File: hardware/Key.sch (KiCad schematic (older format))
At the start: 2 parts

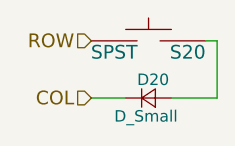
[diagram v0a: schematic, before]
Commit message: Add HWB, breakouts, LED to sch
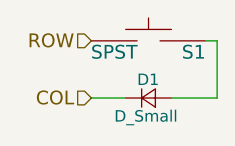
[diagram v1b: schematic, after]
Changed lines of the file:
@@
 $Descr A4 11693 8268
 encoding utf-8
-Sheet 22 66
+Sheet 6 66
 Title ""
 Date ""
@@
 AR Path="/5947FBED/594A0FA7/5940D01B" Ref="S63"  Part="1"
 AR Path="/5947FBED/594A0FB1/5940D01B" Ref="S64"  Part="1"
-F 0 "S20" H 2900 1750 60  0000 R CNN
+F 0 "S1" H 2900 1750 60  0000 R CNN
 F 1 "SPST" H 2500 1750 60  0000 C CNN
 F 2 "keyboard-modules:CHERRY_PCB_100H" H 2650 1900 60  0001 C CNN
@@
 AR Path="/5947FBED/594A0FA7/5940D05E" Ref="D63"  Part="1"
 AR Path="/5947FBED/594A0FB1/5940D05E" Ref="D64"  Part="1"
-F 0 "D20" H 2600 2130 50  0000 L CNN
+F 0 "D1" H 2600 2130 50  0000 L CNN
 F 1 "D_Small" H 2500 1970 50  0000 L CNN
 F 2 "Diodes_SMD:D_1206" V 2650 2050 50  0001 C CNN

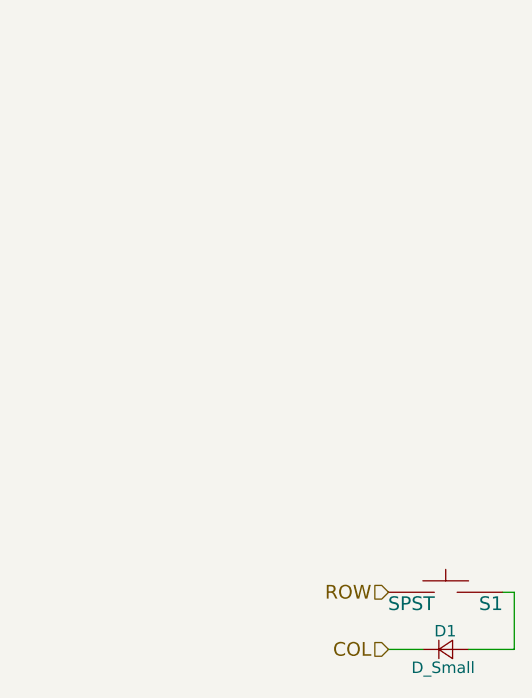
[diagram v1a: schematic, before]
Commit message: Move diodes in script, add big thumb buttons
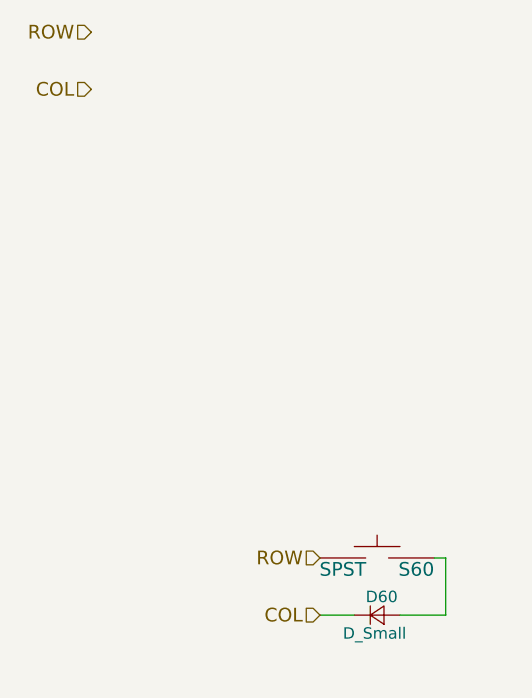
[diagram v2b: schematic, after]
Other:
- moved on the sheet: D60, S60
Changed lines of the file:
@@
 Comment4 ""
 $EndDescr
-Text HLabel 2400 1800 0    60   Input ~ 0
+Text HLabel 2100 1650 0    60   Input ~ 0
 ROW
-Text HLabel 2400 2050 0    60   Input ~ 0
+Text HLabel 2100 1900 0    60   Input ~ 0
 COL
 $Comp
 L SPST S1
 U 1 1 5940D01B
-P 2650 1800
+P 2350 1650
 AR Path="/5947FBED/594A0D2A/5940D01B" Ref="S1"  Part="1"
 AR Path="/5947FBED/594A0D35/5940D01B" Ref="S2"  Part="1"
@@
 AR Path="/5947FBED/594A0F7E/5940D01B" Ref="S59"  Part="1"
 AR Path="/5947FBED/594A0F88/5940D01B" Ref="S60"  Part="1"
-AR Path="/5947FBED/594A0F93/5940D01B" Ref="S61"  Part="1"
-AR Path="/5947FBED/594A0F9D/5940D01B" Ref="S62"  Part="1"
-AR Path="/5947FBED/594A0FA7/5940D01B" Ref="S63"  Part="1"
-AR Path="/5947FBED/594A0FB1/5940D01B" Ref="S64"  Part="1"
-F 0 "S1" H 2900 1750 60  0000 R CNN
-F 1 "SPST" H 2500 1750 60  0000 C CNN
-F 2 "keyboard-modules:CHERRY_PCB_100H" H 2650 1900 60  0001 C CNN
-F 3 "" H 2650 1900 60  0001 C CNN
-	1    2650 1800
+F 0 "S60" H 2600 1600 60  0000 R CNN
+F 1 "SPST" H 2200 1600 60  0000 C CNN
+F 2 "keyboard-modules:CHERRY_PCB_100H" H 2350 1750 60  0001 C CNN
+F 3 "" H 2350 1750 60  0001 C CNN
+	1    2350 1650
 	1    0    0    -1
 $EndComp
@@
 L D_Small D1
 U 1 1 5940D05E
-P 2650 2050
+P 2350 1900
 AR Path="/5947FBED/594A0D2A/5940D05E" Ref="D1"  Part="1"
 AR Path="/5947FBED/594A0D35/5940D05E" Ref="D2"  Part="1"
@@
 AR Path="/5947FBED/594A0F7E/5940D05E" Ref="D59"  Part="1"
 AR Path="/5947FBED/594A0F88/5940D05E" Ref="D60"  Part="1"
-AR Path="/5947FBED/594A0F93/5940D05E" Ref="D61"  Part="1"
-AR Path="/5947FBED/594A0F9D/5940D05E" Ref="D62"  Part="1"
-AR Path="/5947FBED/594A0FA7/5940D05E" Ref="D63"  Part="1"
-AR Path="/5947FBED/594A0FB1/5940D05E" Ref="D64"  Part="1"
-F 0 "D1" H 2600 2130 50  0000 L CNN
-F 1 "D_Small" H 2500 1970 50  0000 L CNN
-F 2 "Diodes_SMD:D_1206" V 2650 2050 50  0001 C CNN
-F 3 "" V 2650 2050 50  0001 C CNN
-	1    2650 2050
+F 0 "D60" H 2300 1980 50  0000 L CNN
+F 1 "D_Small" H 2200 1820 50  0000 L CNN
+F 2 "Diodes_SMD:D_1206" V 2350 1900 50  0001 C CNN
+F 3 "" V 2350 1900 50  0001 C CNN
+	1    2350 1900
 	1    0    0    -1
 $EndComp
 Wire Wire Line
-	2400 2050 2550 2050
+	2100 1900 2250 1900
 Wire Wire Line
-	2900 1800 2950 1800
+	2600 1650 2650 1650
 Wire Wire Line
-	2950 1800 2950 2050
+	2650 1650 2650 1900
 Wire Wire Line
-	2950 2050 2750 2050
+	2650 1900 2450 1900
+Text HLabel 1100 -650 0    60   Input ~ 0
+ROW
+Text HLabel 1100 -400 0    60   Input ~ 0
+COL
 $EndSCHEMATC

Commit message: Fix diodes, Add board edge
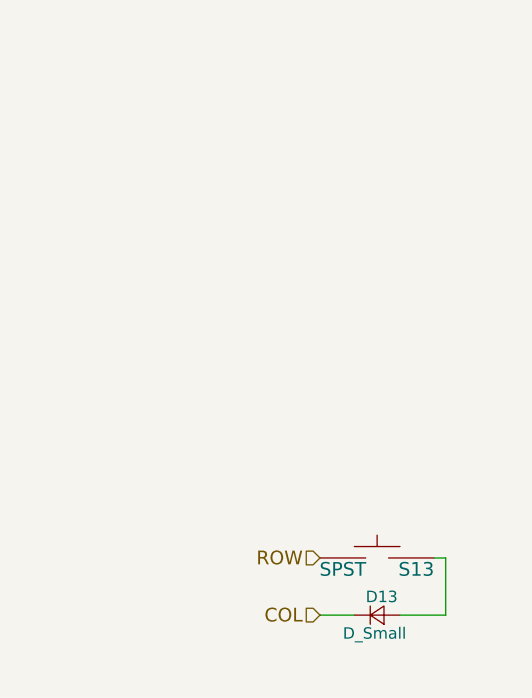
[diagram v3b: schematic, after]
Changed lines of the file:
@@
 $Descr A4 11693 8268
 encoding utf-8
-Sheet 6 66
+Sheet 15 66
 Title ""
 Date ""
@@
 AR Path="/5947FBED/594A0F7E/5940D01B" Ref="S59"  Part="1"
 AR Path="/5947FBED/594A0F88/5940D01B" Ref="S60"  Part="1"
-F 0 "S60" H 2600 1600 60  0000 R CNN
+F 0 "S13" H 2600 1600 60  0000 R CNN
 F 1 "SPST" H 2200 1600 60  0000 C CNN
 F 2 "keyboard-modules:CHERRY_PCB_100H" H 2350 1750 60  0001 C CNN
@@
 AR Path="/5947FBED/594A0F7E/5940D05E" Ref="D59"  Part="1"
 AR Path="/5947FBED/594A0F88/5940D05E" Ref="D60"  Part="1"
-F 0 "D60" H 2300 1980 50  0000 L CNN
+F 0 "D13" H 2300 1980 50  0000 L CNN
 F 1 "D_Small" H 2200 1820 50  0000 L CNN
 F 2 "Diodes_SMD:D_1206" V 2350 1900 50  0001 C CNN
@@
 Wire Wire Line
 	2650 1900 2450 1900
-Text HLabel 1100 -650 0    60   Input ~ 0
-ROW
-Text HLabel 1100 -400 0    60   Input ~ 0
-COL
 $EndSCHEMATC

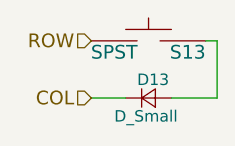
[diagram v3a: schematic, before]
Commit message: Update expansion pads to be SMD
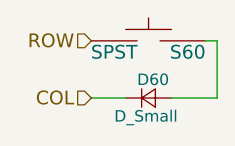
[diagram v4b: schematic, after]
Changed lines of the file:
@@
 LIBS:valves
 LIBS:keyboard-cache
-EELAYER 25 0
+EELAYER 26 0
 EELAYER END
 $Descr A4 11693 8268
@@
 AR Path="/5947FBED/594A0F7E/5940D01B" Ref="S59"  Part="1"
 AR Path="/5947FBED/594A0F88/5940D01B" Ref="S60"  Part="1"
-F 0 "S13" H 2600 1600 60  0000 R CNN
+F 0 "S60" H 2600 1600 60  0000 R CNN
 F 1 "SPST" H 2200 1600 60  0000 C CNN
 F 2 "keyboard-modules:CHERRY_PCB_100H" H 2350 1750 60  0001 C CNN
@@
 AR Path="/5947FBED/594A0F7E/5940D05E" Ref="D59"  Part="1"
 AR Path="/5947FBED/594A0F88/5940D05E" Ref="D60"  Part="1"
-F 0 "D13" H 2300 1980 50  0000 L CNN
+F 0 "D60" H 2300 1980 50  0000 L CNN
 F 1 "D_Small" H 2200 1820 50  0000 L CNN
 F 2 "Diodes_SMD:D_1206" V 2350 1900 50  0001 C CNN

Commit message: Add 3d models
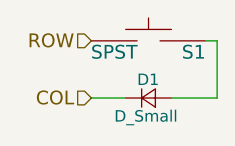
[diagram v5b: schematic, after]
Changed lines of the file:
@@
 LIBS:valves
 LIBS:keyboard-cache
-EELAYER 26 0
+EELAYER 25 0
 EELAYER END
 $Descr A4 11693 8268
 encoding utf-8
-Sheet 15 66
+Sheet 3 66
 Title ""
 Date ""
@@
 AR Path="/5947FBED/594A0F7E/5940D01B" Ref="S59"  Part="1"
 AR Path="/5947FBED/594A0F88/5940D01B" Ref="S60"  Part="1"
-F 0 "S60" H 2600 1600 60  0000 R CNN
+F 0 "S1" H 2600 1600 60  0000 R CNN
 F 1 "SPST" H 2200 1600 60  0000 C CNN
 F 2 "keyboard-modules:CHERRY_PCB_100H" H 2350 1750 60  0001 C CNN
@@
 AR Path="/5947FBED/594A0F7E/5940D05E" Ref="D59"  Part="1"
 AR Path="/5947FBED/594A0F88/5940D05E" Ref="D60"  Part="1"
-F 0 "D60" H 2300 1980 50  0000 L CNN
+F 0 "D1" H 2300 1980 50  0000 L CNN
 F 1 "D_Small" H 2200 1820 50  0000 L CNN
 F 2 "Diodes_SMD:D_1206" V 2350 1900 50  0001 C CNN

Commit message: Start to lay out components
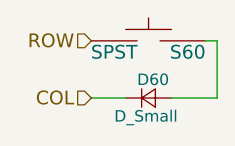
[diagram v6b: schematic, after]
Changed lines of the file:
@@
 LIBS:valves
 LIBS:keyboard-cache
-EELAYER 25 0
+EELAYER 26 0
 EELAYER END
 $Descr A4 11693 8268
@@
 AR Path="/5947FBED/594A0F7E/5940D01B" Ref="S59"  Part="1"
 AR Path="/5947FBED/594A0F88/5940D01B" Ref="S60"  Part="1"
-F 0 "S1" H 2600 1600 60  0000 R CNN
+F 0 "S60" H 2600 1600 60  0000 R CNN
 F 1 "SPST" H 2200 1600 60  0000 C CNN
 F 2 "keyboard-modules:CHERRY_PCB_100H" H 2350 1750 60  0001 C CNN
@@
 AR Path="/5947FBED/594A0F7E/5940D05E" Ref="D59"  Part="1"
 AR Path="/5947FBED/594A0F88/5940D05E" Ref="D60"  Part="1"
-F 0 "D1" H 2300 1980 50  0000 L CNN
+F 0 "D60" H 2300 1980 50  0000 L CNN
 F 1 "D_Small" H 2200 1820 50  0000 L CNN
 F 2 "Diodes_SMD:D_1206" V 2350 1900 50  0001 C CNN

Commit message: More routing
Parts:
- D1: footprint Diodes_SMD:D_1206 -> d_mod:D_1206
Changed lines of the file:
@@
 AR Path="/5947FBED/594A0F7E/5940D01B" Ref="S59"  Part="1"
 AR Path="/5947FBED/594A0F88/5940D01B" Ref="S60"  Part="1"
-F 0 "S60" H 2600 1600 60  0000 R CNN
+F 0 "S2" H 2600 1600 60  0000 R CNN
 F 1 "SPST" H 2200 1600 60  0000 C CNN
 F 2 "keyboard-modules:CHERRY_PCB_100H" H 2350 1750 60  0001 C CNN
@@
 AR Path="/5947FBED/594A0F7E/5940D05E" Ref="D59"  Part="1"
 AR Path="/5947FBED/594A0F88/5940D05E" Ref="D60"  Part="1"
-F 0 "D60" H 2300 1980 50  0000 L CNN
+F 0 "D2" H 2300 1980 50  0000 L CNN
 F 1 "D_Small" H 2200 1820 50  0000 L CNN
-F 2 "Diodes_SMD:D_1206" V 2350 1900 50  0001 C CNN
+F 2 "d_mod:D_1206" V 2350 1900 50  0001 C CNN
 F 3 "" V 2350 1900 50  0001 C CNN
 	1    2350 1900

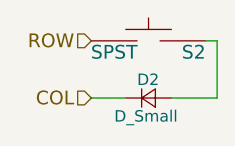
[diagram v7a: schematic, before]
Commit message: Update parts after starting sourcing
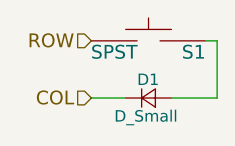
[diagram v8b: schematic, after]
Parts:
- D1: footprint d_mod:D_1206 -> Diodes_SMD:D_SOD-123
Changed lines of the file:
@@
 AR Path="/5947FBED/594A0F7E/5940D01B" Ref="S59"  Part="1"
 AR Path="/5947FBED/594A0F88/5940D01B" Ref="S60"  Part="1"
-F 0 "S2" H 2600 1600 60  0000 R CNN
+F 0 "S1" H 2600 1600 60  0000 R CNN
 F 1 "SPST" H 2200 1600 60  0000 C CNN
 F 2 "keyboard-modules:CHERRY_PCB_100H" H 2350 1750 60  0001 C CNN
@@
 AR Path="/5947FBED/594A0F7E/5940D05E" Ref="D59"  Part="1"
 AR Path="/5947FBED/594A0F88/5940D05E" Ref="D60"  Part="1"
-F 0 "D2" H 2300 1980 50  0000 L CNN
+F 0 "D1" H 2300 1980 50  0000 L CNN
 F 1 "D_Small" H 2200 1820 50  0000 L CNN
-F 2 "d_mod:D_1206" V 2350 1900 50  0001 C CNN
+F 2 "Diodes_SMD:D_SOD-123" V 2350 1900 50  0001 C CNN
 F 3 "" V 2350 1900 50  0001 C CNN
 	1    2350 1900
